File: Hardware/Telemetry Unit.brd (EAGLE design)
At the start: 50.8 x 63.5 mm, 56 parts, among them IC1 MEGA128-A, IC2 FT232RL, J2 503182-1852, J3 10118193-0001LF, Q1 10MHz, U1 MPL3115A2, U2 AP65111A, U3 LSM6DS3

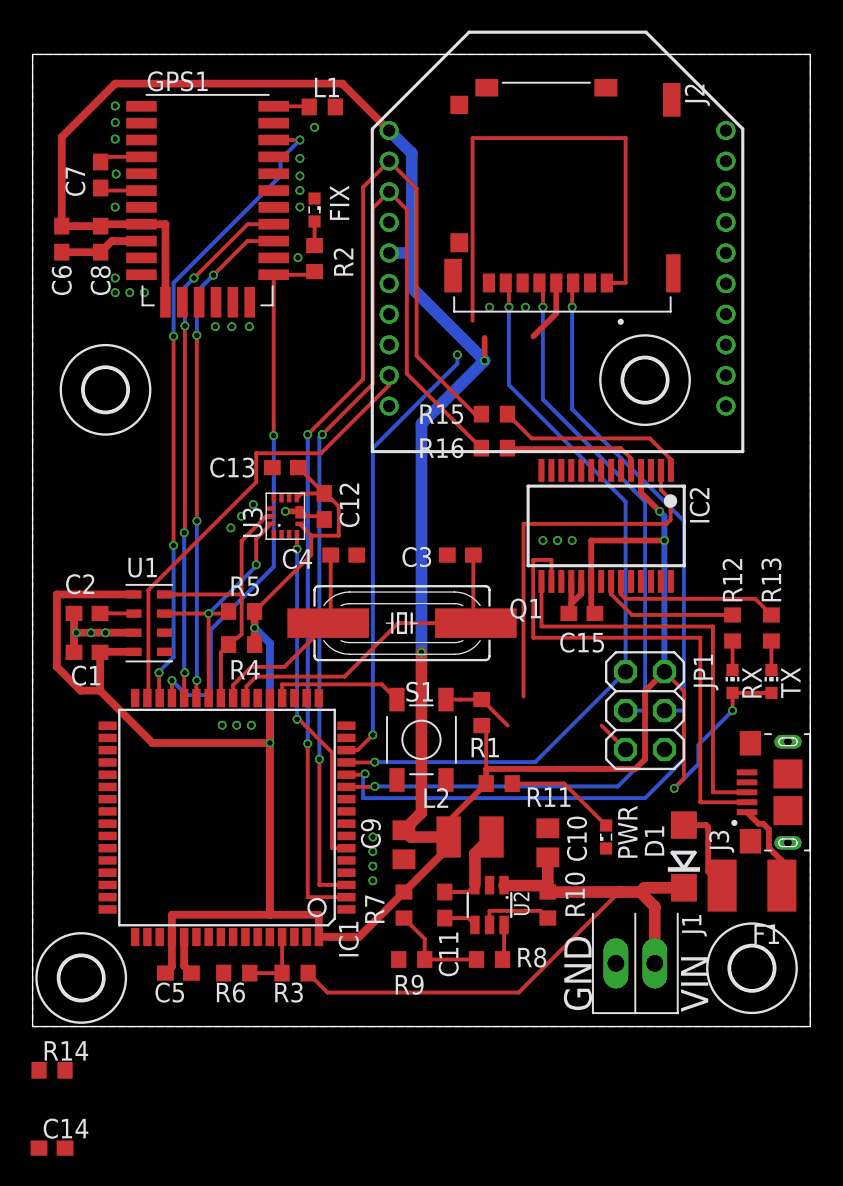
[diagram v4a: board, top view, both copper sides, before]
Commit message: Reroute replaced components and add logo
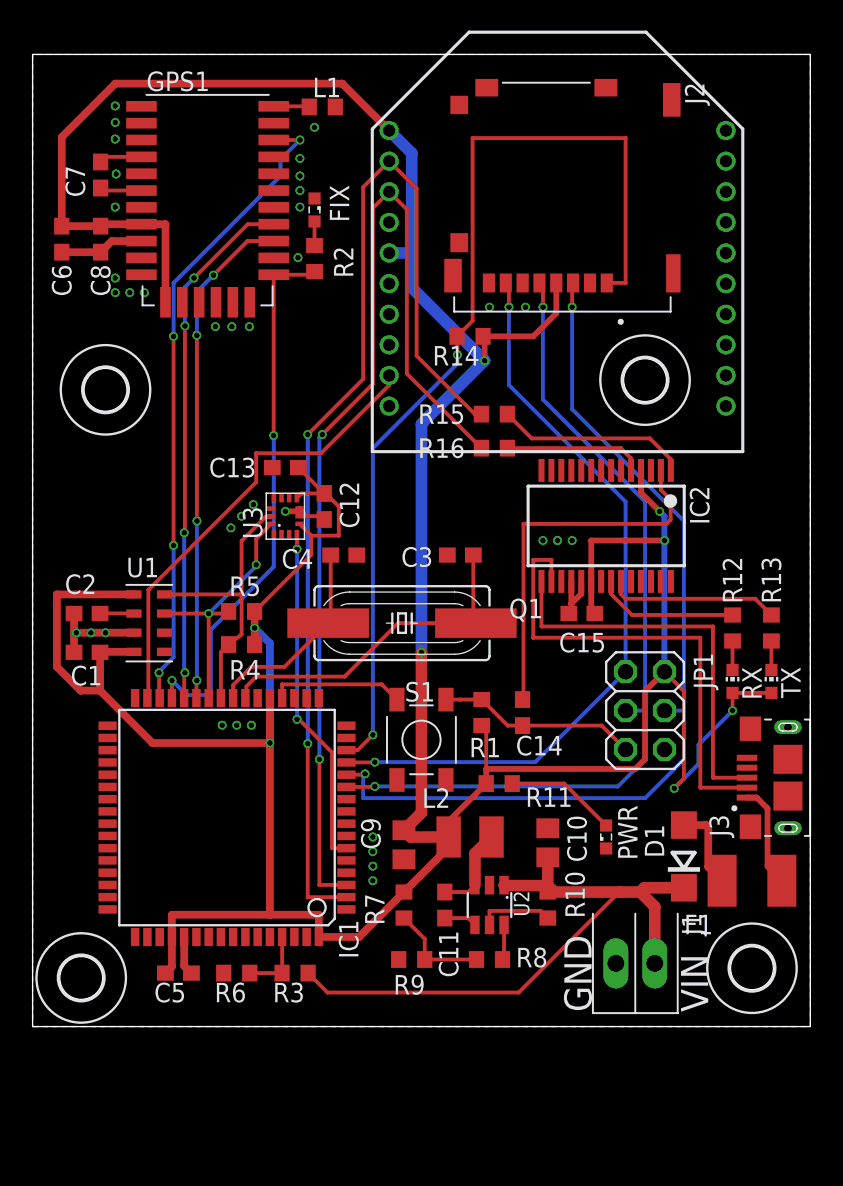
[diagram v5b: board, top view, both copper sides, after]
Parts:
- moved R14 55.2 mm to (28.6, 45.1), turned to 180 degrees
- moved C14 41.9 mm to (32.0, 20.5), turned to 270 degrees
- moved J3 0.95 mm to (49.3, 16.3)
- moved F1 0.32 mm to (47.0, 9.53)
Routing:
- net RST2: track 6.95 -> 13.1 mm
- net +3V3: track 268.2 -> 271.6 mm
- net CS_SD: track 61.9 -> 64.5 mm
- net N$13: track 27.2 -> 26.2 mm
- net N$11: track 32.4 -> 31.4 mm
- net N$22: track 5.92 -> 6.75 mm
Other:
- board text added: "MMD V1.0"

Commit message: Most minor updates and some rerouting
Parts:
- R11, R2: value 470 -> 1k
- R16: value 10k -> 330
- moved R16 21.6 mm to (41.9, 19.7), turned to 270 degrees
- moved R15 15.1 mm to (44.5, 35.2), turned to 270 degrees
- moved C15 11.7 mm to (38.5, 38.4)
- moved R1 3.52 mm to (32.6, 19.3)
- moved U$3 3.24 mm to (43.2, 41.6)
- moved R11 3.23 mm to (33.7, 15.3)
- moved J2 3.18 mm to (37.1, 53.0), turned to 0 degrees
- moved JP1 2.54 mm to (37.5, 20.6)
- moved R14 2.54 mm to (31.1, 45.1)
- moved XB1 2.54 mm to (36.8, 49.5)
- moved S1 2.48 mm to (27.3, 20.3), turned to 180 degrees
- moved C14 2.01 mm to (32.6, 22.4)
- moved L1 1.27 mm to (20.2, 60.1)
- moved C6 1.27 mm to (3.17, 51.4)
- moved C7 1.27 mm to (5.71, 55.6)
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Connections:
- removed net N$21: IC2.5, R16.1
- removed net RST2: C14.2, JP1.5, R1.2, S1.P$4
- removed net RX0: IC1.2, R15.2, XB1.2
- removed net TX0: IC1.3, R16.2, XB1.3
- new net ALT_INT: IC1.6, U1.6
- new net PDI: JP1.4, R16.1
- new net RX0/PDI: IC1.2, R15.2, R16.2, XB1.2
- new net TX0/PDO: IC1.3, IC2.5, JP1.1, XB1.3
- net !RST: now also C14.2, JP1.5, R1.2, S1.P2@1, S1.P2@2; no longer S1.P$3
- net +3V3: no longer IC2.20
- net ACCEL_INT: now also IC1.7; no longer IC1.6
- net CS_SD: now also J2.2; no longer J2.1
- net GND: now also S1.P1@1, S1.P1@2, U3.1, U3.12, U3.2, U3.3; no longer IC2.19, S1.P$1, S1.P$2
- net MISO: no longer JP1.1
- net MOSI: no longer JP1.4
- net V_USB: now also IC2.20
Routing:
- net RX0: track 72.1 -> 0.00 mm, vias 2 -> 0
- net TX0: track 68.2 -> 0.00 mm, vias 2 -> 0
- net MOSI: track 60.3 -> 1.22 mm, vias 2 -> 1
- net MISO: track 49.3 -> 1.22 mm, vias 2 -> 1
- net RX0/PDI: track 0.00 -> 45.6 mm, vias 0 -> 3
- net TX0/PDO: track 0.00 -> 41.1 mm, vias 0 -> 2
- net CS_SD: track 64.5 -> 23.7 mm, vias 2 -> 1
- net +3V3: track 271.6 -> 244.9 mm, vias 8 -> 6
- net ALT_INT: track 0.00 -> 24.9 mm, vias 0 -> 2
- net RST2: track 13.1 -> 0.00 mm
- net SCK: track 55.5 -> 44.8 mm, vias 2 -> 1
- net N$20: track 12.6 -> 3.00 mm
- net !RST: track 8.81 -> 18.1 mm
- net N$21: track 9.14 -> 0.00 mm
- net N$14: track 7.27 -> 3.86 mm
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
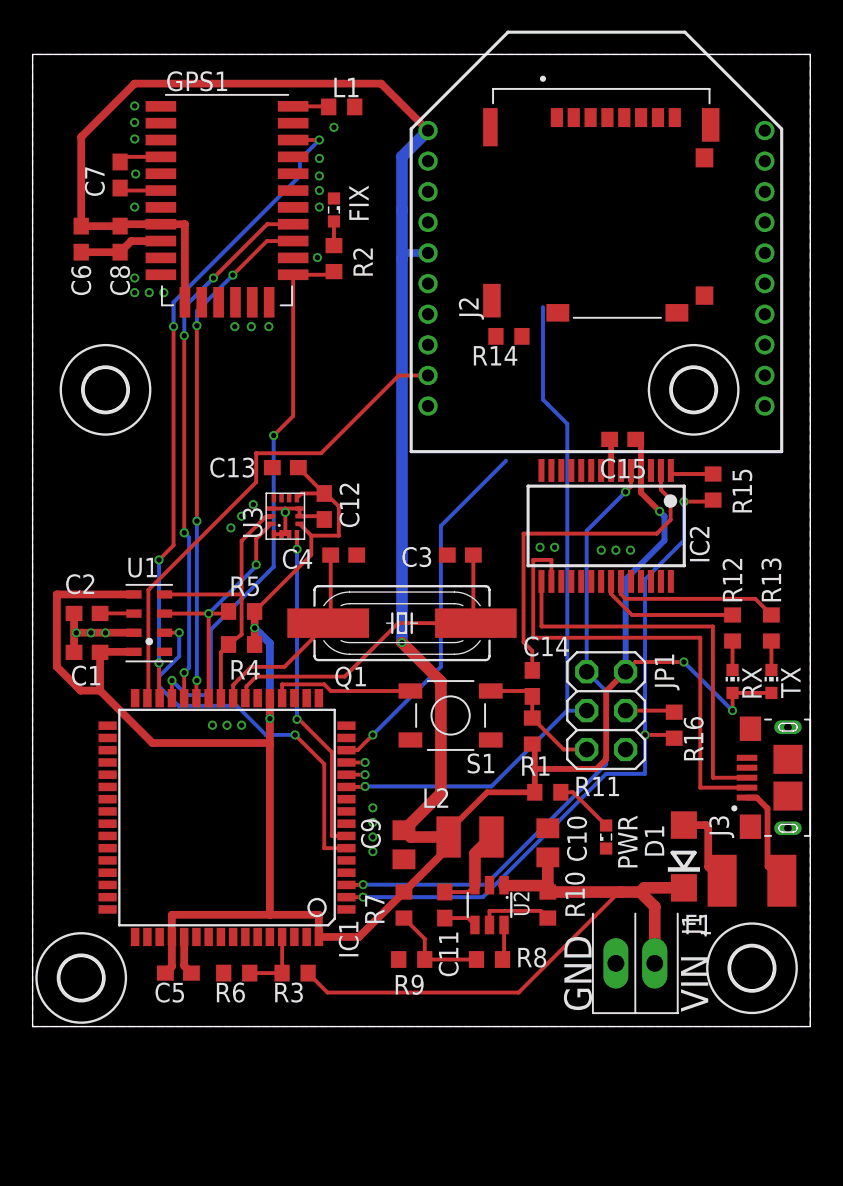
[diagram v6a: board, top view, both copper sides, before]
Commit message: New diode, layer cleanup, update silk
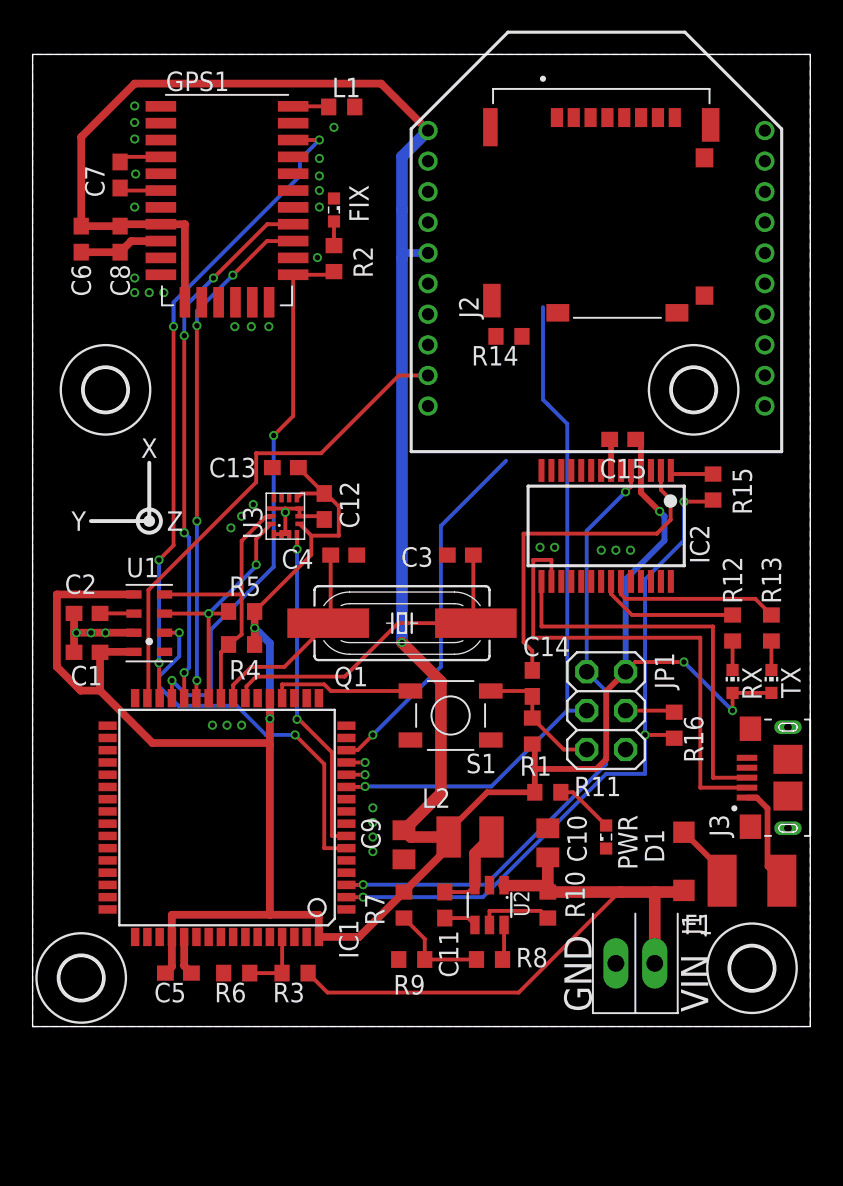
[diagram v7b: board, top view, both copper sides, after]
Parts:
- D1: device diode:DO214AC -> diode:SOD123
- moved D1 0.32 mm to (42.5, 10.8)
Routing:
- net V_USB: track 5.52 -> 4.20 mm
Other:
- board text added: "MMD V1.1"
- board text added: "X"
- board text added: "Y"
- board text added: "Z"
- board text removed: "MMD V1.0"

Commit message: Replace voltage regulator, reroute all
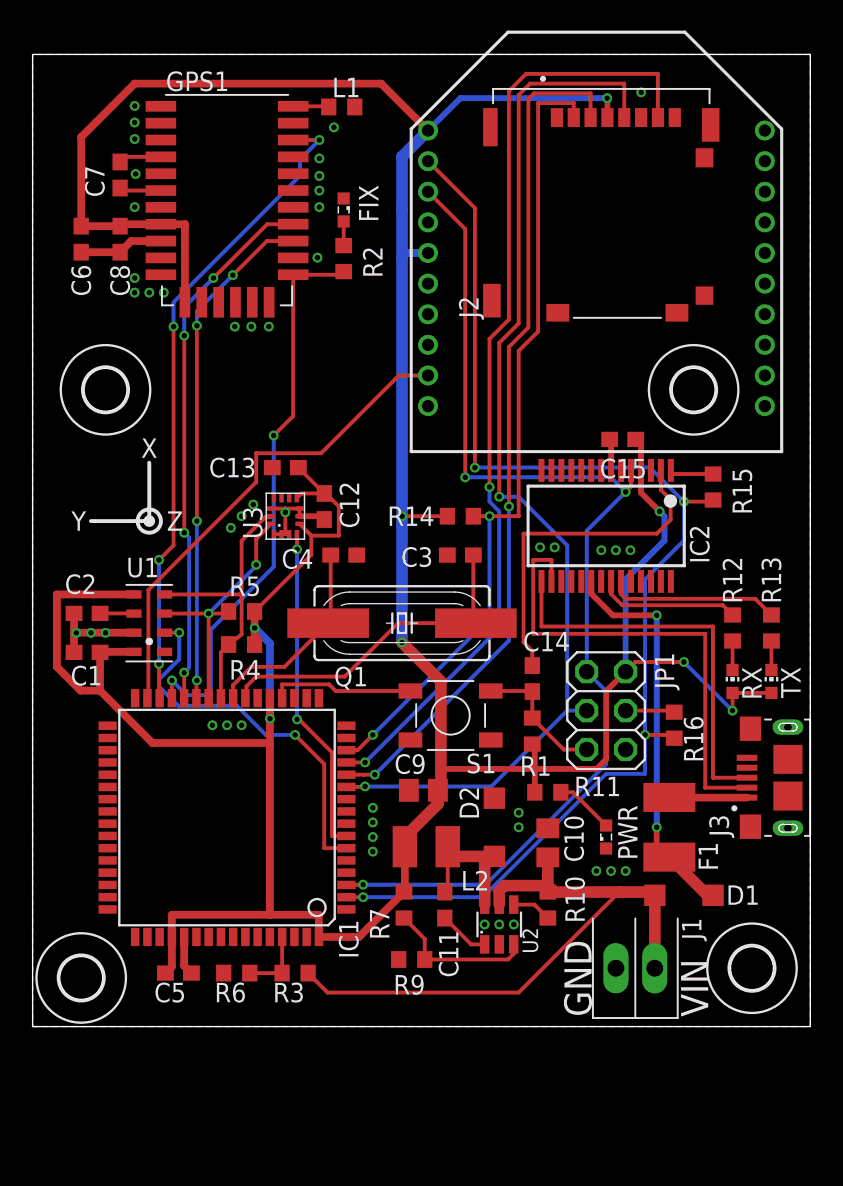
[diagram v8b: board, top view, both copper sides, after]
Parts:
- removed R8: 59k, resistor:R0603
- added D2: (no value), diode:SOD123
- C11: value 22p -> 100n
- U2: value AP65111A -> AOZ1280
- moved R14 12.2 mm to (27.9, 33.3), turned to 0 degrees
- moved F1 6.43 mm to (41.6, 13.0), turned to 270 degrees
- moved C9 3.78 mm to (25.5, 15.4), turned to 180 degrees
- moved L2 2.93 mm to (25.7, 11.7)
- moved D1 2.22 mm to (42.5, 8.57), turned to 0 degrees
- moved U2 1.42 mm to (30.5, 6.67), turned to 0 degrees
- moved FIX 0.64 mm to (20.3, 53.3)
- moved R2 0.64 mm to (20.3, 50.2)
- moved J1 0.32 mm to (39.4, 3.81)
- moved C14 0.32 mm to (32.6, 22.7)
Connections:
- removed net N$8: R7.2, R8.2, R9.1
- net GND: now also D2.A
- net N$10: now also R7.2, R9.1, U2.3; no longer R8.1, U2.6
- net N$12: now also U2.1; no longer U2.4
- net N$7: now also D2.C, U2.6; no longer U2.3
- net N$9: now also U2.4; no longer U2.5
- net VBAT: now also U2.5; no longer U2.1
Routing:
- net MISO: track 1.22 -> 62.5 mm, vias 1 -> 2
- net MOSI: track 1.22 -> 55.9 mm, vias 1 -> 2
- net RX0/PDI: track 45.6 -> 81.5 mm, vias 3 -> 4
- net TX0/PDO: track 41.1 -> 71.7 mm, vias 2 -> 3
- net CS_SD: track 23.7 -> 53.3 mm, vias 1 -> 2
- net SCK: track 44.8 -> 70.5 mm, vias 1 -> 2
- net V_USB: track 4.20 -> 25.7 mm, vias 0 -> 2
- net +3V3: track 244.9 -> 256.4 mm, vias 6 -> 8
- net N$10: track 2.30 -> 9.85 mm
- net N$8: track 6.65 -> 0.00 mm
- net N$7: track 5.75 -> 9.50 mm
- net N$9: track 4.92 -> 2.59 mm
- net N$22: track 6.75 -> 5.08 mm
- net N$12: track 2.16 -> 3.32 mm
- net FIX: track 36.6 -> 37.3 mm
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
